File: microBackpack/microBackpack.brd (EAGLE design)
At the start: 121.9 x 76.2 mm, 61 parts, among them IC1 LM324D, IC2 LM324D, J2 USB_B_PTH, J4 2X6 FEMALE, U1 ATMEGA328P_TQFP, U2 5VREG-HS, U3 CP2102N-QFN24, U4 TVS_DIODE_4PK, U5 MCP4728, U6 78L09F, U7 TVS_DIODE_4PK

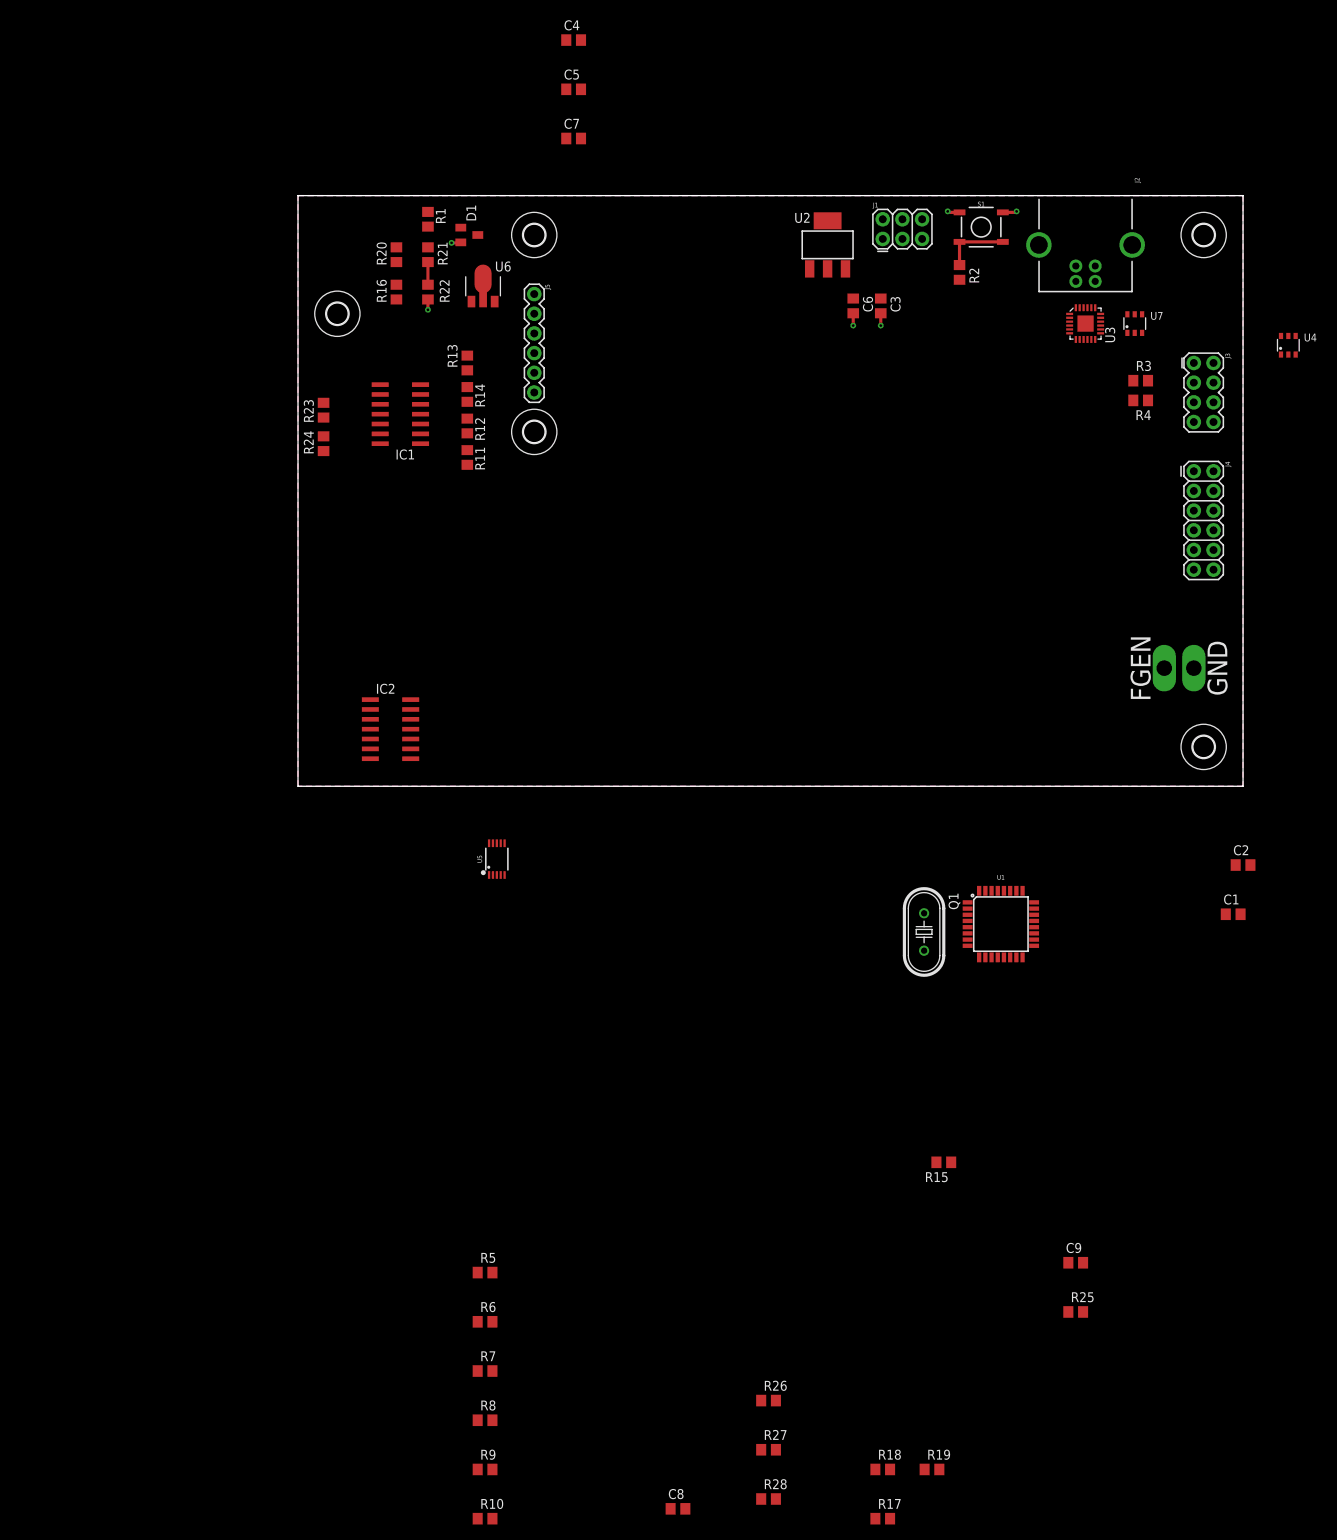
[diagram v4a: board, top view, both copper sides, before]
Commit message: Spec'd header part. Added DIO protection diodes and resistors. Significantly more routing done
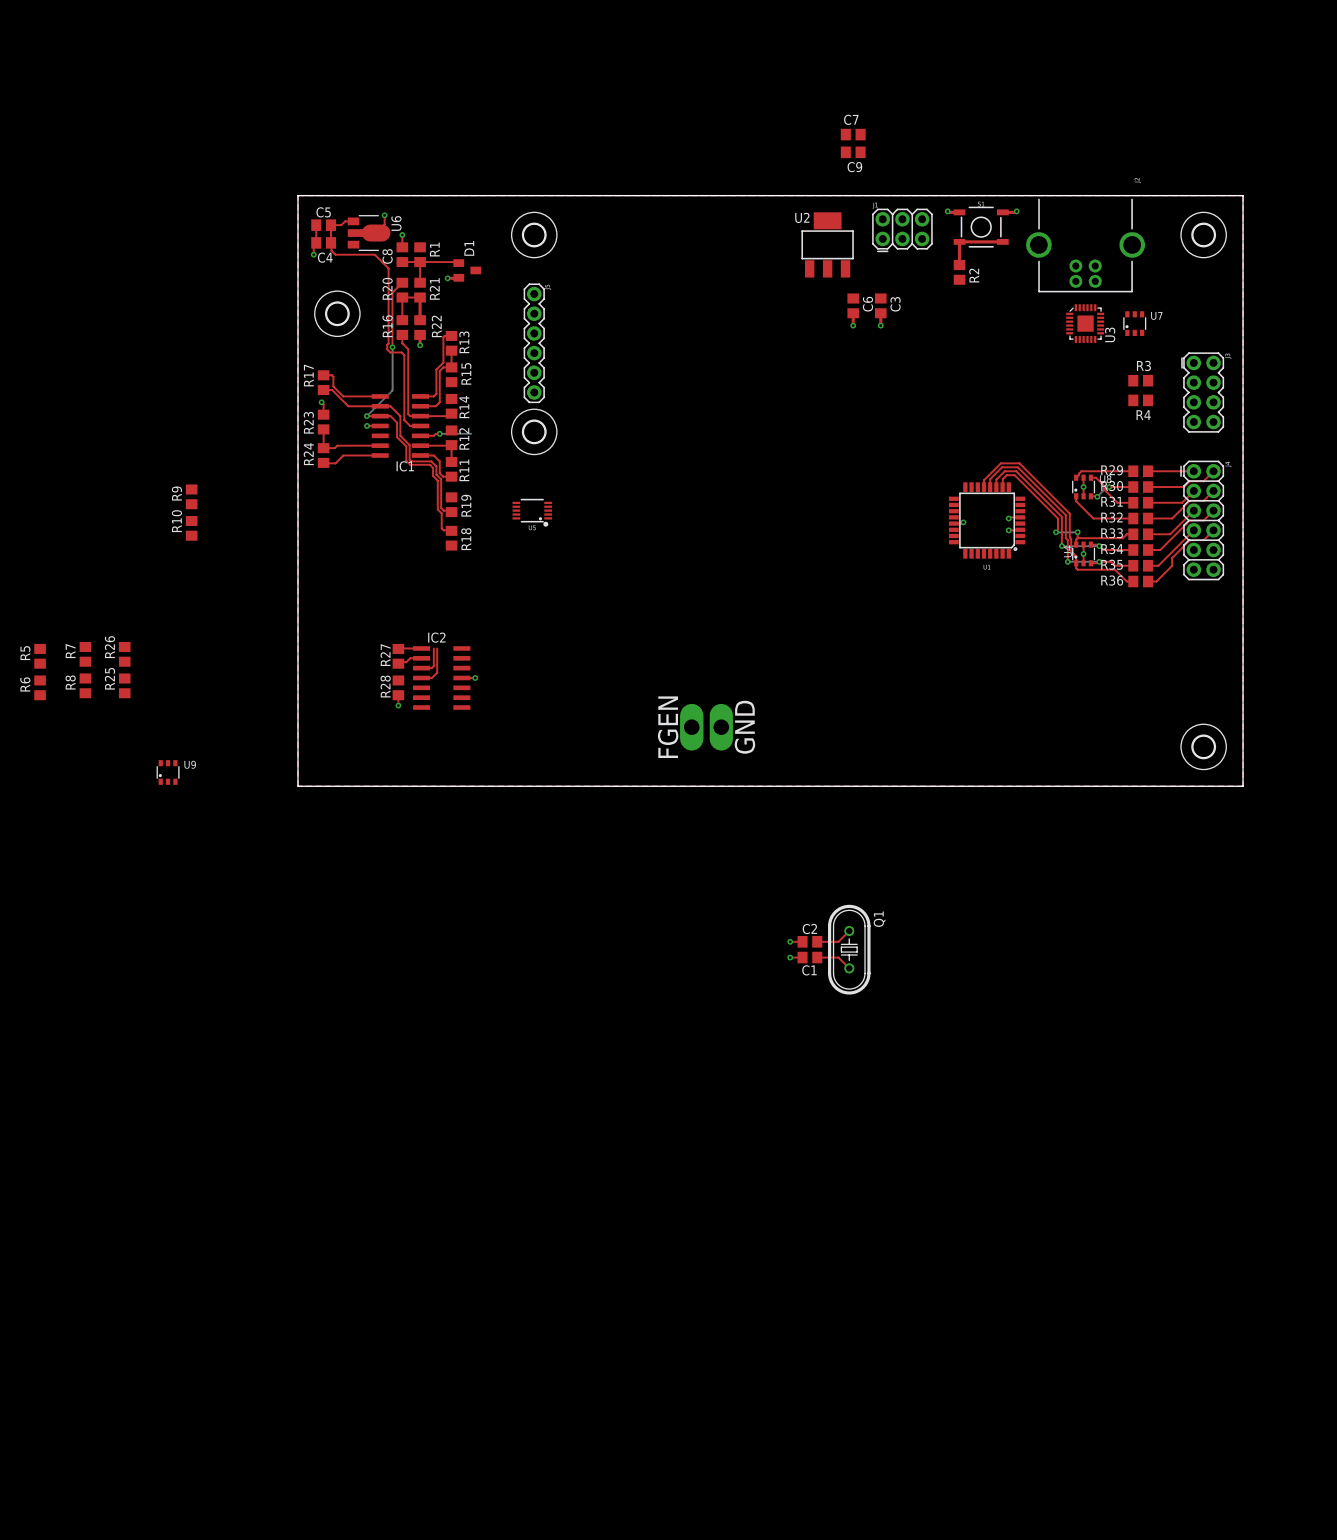
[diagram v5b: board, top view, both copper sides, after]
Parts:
- added R29, R30, R31, R32, R33, R34, R35, R36: 10, rcl:R0805
- added U8, U9: TVS_DIODE_4PK, microBackpackLib:SOT457
- moved C8 165.7 mm to (13.5, 68.6), turned to 90 degrees
- moved R17 163.3 mm to (3.30, 52.1), turned to 90 degrees
- moved R25 146.9 mm to (-22.4, 13.0), turned to 90 degrees
- moved C9 146.1 mm to (71.6, 81.8)
- moved R19 139.0 mm to (19.8, 36.3), turned to 270 degrees
- moved R10 133.2 mm to (-13.7, 33.3), turned to 90 degrees
- moved R18 132.4 mm to (19.8, 32.0), turned to 90 degrees
- moved R9 131.1 mm to (-13.7, 37.3), turned to 90 degrees
- moved R26 127.1 mm to (-22.4, 17.0), turned to 90 degrees
- moved R15 119.8 mm to (19.8, 53.1), turned to 90 degrees
- moved R28 115.0 mm to (13.0, 12.7), turned to 270 degrees
- moved R27 113.0 mm to (13.0, 16.8), turned to 270 degrees
- moved R8 107.9 mm to (-27.4, 13.0), turned to 90 degrees
- moved R7 105.9 mm to (-27.4, 17.0), turned to 90 degrees
- moved R6 99.9 mm to (-33.3, 12.7), turned to 90 degrees
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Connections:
- net N$4 renamed USB_GND
- new net DIO0_PROT: R29.2, U1.32, U8.6
- new net DIO1_PROT: R30.2, U1.1, U8.3
- new net DIO2_PROT: R31.2, U1.2, U8.4
- new net DIO3_PROT: R32.2, U1.9, U8.1
- new net DIO4_PROT: R33.2, U1.10, U4.6
- new net DIO5_PROT: R34.2, U1.11, U4.4
- new net DIO6_PROT: R35.2, U1.12, U4.3
- new net DIO7_PROT: R36.2, U1.13, U4.1
- net ADC0: now also U9.6
- net ADC1: now also U9.4
- net ADC6: now also U9.3
- net ADC7: now also U9.1
- net DIO0: now also R29.1; no longer U1.32
- net DIO1: now also R30.1; no longer U1.1
- net DIO2: now also R31.1; no longer U1.2
- net DIO3: now also R32.1; no longer U1.9
- net DIO4: now also R33.1; no longer U1.10
- net DIO5: now also R34.1; no longer U1.11
- net DIO6: now also R35.1; no longer U1.12
- net DIO7: now also R36.1; no longer U1.13
- net GND: now also J4.11, U4.2, U4.5, U8.2, U8.5, U9.2, U9.5
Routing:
- net N$15: track 0.00 -> 41.7 mm, vias 0 -> 2
- net 9V: track 0.00 -> 38.6 mm
- net DIO7_PROT: track 0.00 -> 31.0 mm
- net DIO6_PROT: track 0.00 -> 29.9 mm, vias 0 -> 2
- net N$14: track 0.00 -> 28.4 mm
- net GND: track 9.14 -> 36.5 mm, vias 6 -> 20
- net DIO5_PROT: track 0.00 -> 26.7 mm, vias 0 -> 2
- net DIO4_PROT: track 0.00 -> 24.4 mm, vias 0 -> 2
- net N$10: track 0.00 -> 16.4 mm
- net DIO7: track 0.00 -> 11.8 mm
- net ADC0: track 0.00 -> 11.0 mm
- net N$9: track 0.00 -> 10.6 mm
- net DIO5: track 0.00 -> 10.6 mm
- net 4V_REF: track 0.00 -> 10.0 mm
- net DIO3: track 0.00 -> 9.92 mm
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
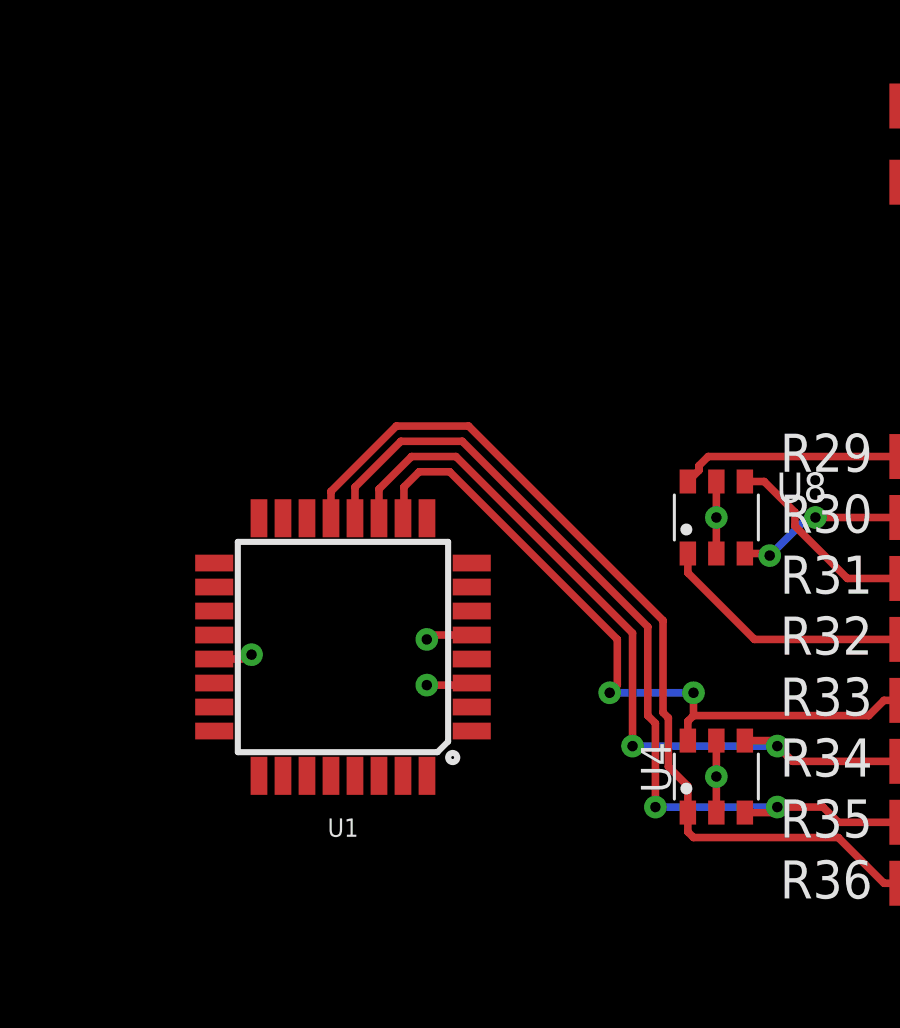
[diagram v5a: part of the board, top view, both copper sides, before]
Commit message: Rotated MCU to a 45
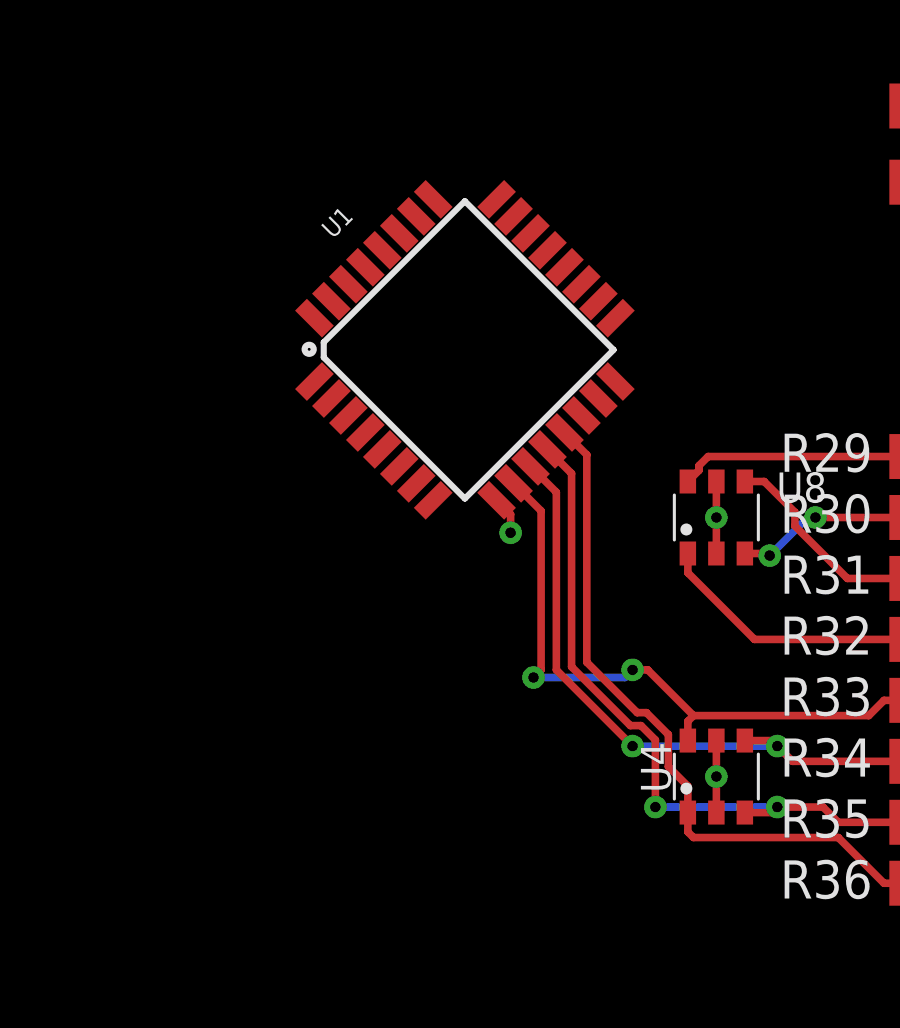
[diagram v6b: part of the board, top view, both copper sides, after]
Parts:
- moved U1 10.7 mm to (93.0, 44.2), turned to 45 degrees
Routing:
- net DIO7_PROT: track 31.0 -> 23.3 mm
- net DIO6_PROT: track 29.9 -> 23.4 mm
- net DIO5_PROT: track 26.7 -> 21.3 mm
- net GND: track 36.5 -> 32.1 mm, vias 20 -> 17
- net DIO4_PROT: track 24.4 -> 21.3 mm
- net DIO3_PROT: track 9.03 -> 10.3 mm, vias 0 -> 1

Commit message: More routing
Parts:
- moved R25 165.2 mm to (139.4, 46.5)
- moved R26 165.2 mm to (139.4, 50.5)
- moved R5 165.2 mm to (128.5, 50.3)
- moved R6 165.2 mm to (128.5, 46.2)
- moved R7 165.2 mm to (134.4, 50.5)
- moved R8 165.2 mm to (134.4, 46.5)
- moved R10 159.8 mm to (145.5, 46.5)
- moved R9 159.8 mm to (145.5, 50.5)
- moved U9 120.4 mm to (96.5, 42.4)
- moved U5 15.3 mm to (18.8, 25.4), turned to 180 degrees
- moved R29 9.48 mm to (107.4, 31.2)
- moved R31 9.48 mm to (107.4, 27.2)
- moved R33 9.48 mm to (107.4, 23.1)
- moved R34 9.48 mm to (107.4, 21.1)
- moved R35 9.48 mm to (107.4, 19.1)
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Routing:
- net LDAC: track 0.00 -> 11.6 mm, vias 0 -> 2
- net ADC1: track 9.18 -> 17.4 mm
- net DIO0: track 5.91 -> 0.00 mm
- net ADC0: track 11.0 -> 16.3 mm
- net ADC6: track 0.00 -> 5.02 mm
- net DIO1: track 9.29 -> 4.63 mm
- net DIO2: track 6.54 -> 2.16 mm
- net ADC7: track 0.00 -> 3.24 mm
- net DIO3: track 9.92 -> 6.81 mm
- net DIO4: track 7.17 -> 4.31 mm
- net GND: track 32.1 -> 34.5 mm, vias 17 -> 18
- net DIO5: track 10.6 -> 8.96 mm
- net DIO6: track 7.80 -> 6.47 mm
- net DIO7: track 11.8 -> 10.7 mm

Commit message: Added 2nd order filter to FGEN
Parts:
- added C10, C11: 1.5nF, rcl:C0805
- added R37, R38: 10k, rcl:R0805
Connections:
- new net N$12: IC1.12, R37.1
- new net N$4: C10.1, C11.1, R37.2, R38.1
- net DAC_C: now also R38.2; no longer IC1.12
- net FGEN: now also C11.2
- net GND: now also C10.2
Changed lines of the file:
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@@
 <attribute name="VALUE" x="108.077" y="19.558" size="1.27" layer="27" rot="R180"/>
+</element>
+<element name="C10" library="rcl" library_urn="urn:adsk.eagle:library:334" package="C0805" package3d_urn="urn:adsk.eagle:package:23617/2" value="1.5nF" x="5.842" y="34.29" smashed="yes">
+<attribute name="NAME" x="4.572" y="35.56" size="1.27" layer="25"/>
+<attribute name="POPULARITY" value="63" x="5.842" y="34.29" size="1.778" layer="27" display="off"/>
+<attribute name="SPICEPREFIX" value="C" x="5.842" y="34.29" size="1.778" layer="27" display="off"/>
+<attribute name="VALUE" x="4.572" y="31.75" size="1.27" layer="27"/>
+</element>
+<element name="C11" library="rcl" library_urn="urn:adsk.eagle:library:334" package="C0805" package3d_urn="urn:adsk.eagle:package:23617/2" value="1.5nF" x="5.842" y="27.94" smashed="yes">
+<attribute name="NAME" x="4.572" y="29.21" size="1.27" layer="25"/>
+<attribute name="POPULARITY" value="63" x="5.842" y="27.94" size="1.778" layer="27" display="off"/>
+<attribute name="SPICEPREFIX" value="C" x="5.842" y="27.94" size="1.778" layer="27" display="off"/>
+<attribute name="VALUE" x="4.572" y="25.4" size="1.27" layer="27"/>
+</element>
+<element name="R37" library="rcl" library_urn="urn:adsk.eagle:library:334" package="R0805" package3d_urn="urn:adsk.eagle:package:23553/2" value="10k" x="5.842" y="21.59" smashed="yes">
+<attribute name="NAME" x="5.207" y="22.86" size="1.27" layer="25"/>
+<attribute name="POPULARITY" value="85" x="5.842" y="21.59" size="1.778" layer="27" display="off"/>
+<attribute name="SPICEPREFIX" value="R" x="5.842" y="21.59" size="1.778" layer="27" display="off"/>
+<attribute name="VALUE" x="5.207" y="19.05" size="1.27" layer="27"/>
+</element>
+<element name="R38" library="rcl" library_urn="urn:adsk.eagle:library:334" package="R0805" package3d_urn="urn:adsk.eagle:package:23553/2" value="10k" x="5.842" y="15.24" smashed="yes">
+<attribute name="NAME" x="5.207" y="16.51" size="1.27" layer="25"/>
+<attribute name="POPULARITY" value="85" x="5.842" y="15.24" size="1.778" layer="27" display="off"/>
+<attribute name="SPICEPREFIX" value="R" x="5.842" y="15.24" size="1.778" layer="27" display="off"/>
+<attribute name="VALUE" x="5.207" y="12.7" size="1.27" layer="27"/>
 </element>
 </elements>
@@
 <via x="96.52" y="42.418" extent="1-16" drill="0.35"/>
 <wire x1="96.52" y1="41.218" x2="96.52" y2="42.418" width="0.254" layer="1"/>
-<wire x1="118.11" y1="46.99" x2="118.11" y2="49.53" width="0" layer="19" extent="1-1"/>
+<contactref element="C10" pad="2"/>
+<wire x1="139.446" y1="45.532" x2="145.542" y2="45.532" width="0" layer="19" extent="1-1"/>
+<wire x1="134.366" y1="45.532" x2="139.446" y2="45.532" width="0" layer="19" extent="1-1"/>
+<wire x1="128.524" y1="45.278" x2="134.366" y2="45.532" width="0" layer="19" extent="1-1"/>
+<wire x1="118.11" y1="46.99" x2="128.524" y2="45.278" width="0" layer="19" extent="1-1"/>
+<wire x1="118.11" y1="49.53" x2="118.11" y2="46.99" width="0" layer="19" extent="1-1"/>
 <wire x1="118.11" y1="27.94" x2="118.11" y2="46.99" width="0" layer="19" extent="1-1"/>
 <wire x1="115.57" y1="27.94" x2="118.11" y2="27.94" width="0" layer="19" extent="1-1"/>
@@
 <wire x1="2.352" y1="72.39" x2="7.417" y2="71.374" width="0" layer="19" extent="1-1"/>
 <wire x1="19.796" y1="23.35" x2="19.812" y2="45.908" width="0" layer="19" extent="1-1"/>
-<wire x1="22.86" y1="13.97" x2="19.796" y2="23.35" width="0" layer="19" extent="1-1"/>
+<wire x1="21.142" y1="13.97" x2="19.796" y2="23.35" width="0" layer="19" extent="1-1"/>
 <wire x1="12.954" y1="11.75" x2="21.142" y2="13.97" width="0" layer="19" extent="1-1"/>
-<wire x1="145.542" y1="45.532" x2="3.302" y2="47.94" width="0" layer="19" extent="1-1"/>
-<wire x1="139.446" y1="45.532" x2="145.542" y2="45.532" width="0" layer="19" extent="1-1"/>
-<wire x1="134.366" y1="45.532" x2="139.446" y2="45.532" width="0" layer="19" extent="1-1"/>
-<wire x1="128.524" y1="45.278" x2="134.366" y2="45.532" width="0" layer="19" extent="1-1"/>
 <wire x1="54.61" y1="7.62" x2="22.86" y2="13.97" width="0" layer="19" extent="1-1"/>
 <wire x1="63.5" y1="-20.066" x2="54.61" y2="7.62" width="0" layer="19" extent="1-1"/>
 <wire x1="65.09" y1="-22.098" x2="65.09" y2="-20.066" width="0" layer="19" extent="1-1"/>
+<wire x1="6.792" y1="34.29" x2="12.954" y2="10.414" width="0" layer="19" extent="1-1"/>
 </signal>
 <signal name="MISO">
@@
 <signal name="DAC_C">
 <contactref element="U5" pad="8"/>
-<contactref element="IC1" pad="12"/>
-<wire x1="10.608" y1="45.212" x2="18.796" y2="23.35" width="0" layer="19" extent="1-1"/>
+<contactref element="R38" pad="2"/>
+<wire x1="18.796" y1="23.35" x2="6.792" y2="15.24" width="0" layer="19" extent="1-1"/>
 </signal>
 <signal name="DAC_D">
@@
 <wire x1="4.826" y1="41.656" x2="3.368" y2="41.656" width="0.254" layer="1"/>
 <wire x1="3.368" y1="41.656" x2="3.302" y2="41.722" width="0.254" layer="1"/>
-<wire x1="10.608" y1="42.672" x2="50.8" y2="7.62" width="0" layer="19" extent="1-1"/>
+<contactref element="C11" pad="2"/>
+<wire x1="3.368" y1="41.656" x2="6.792" y2="27.94" width="0" layer="19" extent="1-1"/>
+<wire x1="50.8" y1="7.62" x2="10.608" y2="42.672" width="0" layer="19" extent="1-1"/>
 </signal>
 <signal name="N$11">
@@
 <wire x1="98.4758" y1="20.9042" x2="99.126" y2="20.254" width="0.254" layer="1"/>
 </signal>
+<signal name="N$4">
+<contactref element="R37" pad="2"/>
+<contactref element="C10" pad="1"/>
+<contactref element="R38" pad="1"/>
+<contactref element="C11" pad="1"/>
+<wire x1="6.792" y1="21.59" x2="4.892" y2="15.24" width="0" layer="19" extent="1-1"/>
+<wire x1="4.892" y1="27.94" x2="6.792" y2="21.59" width="0" layer="19" extent="1-1"/>
+<wire x1="4.892" y1="34.29" x2="4.892" y2="27.94" width="0" layer="19" extent="1-1"/>
+</signal>
+<signal name="N$12">
+<contactref element="R37" pad="1"/>
+<contactref element="IC1" pad="12"/>
+<wire x1="4.892" y1="21.59" x2="10.608" y2="45.212" width="0" layer="19" extent="1-1"/>
+</signal>
 </signals>
